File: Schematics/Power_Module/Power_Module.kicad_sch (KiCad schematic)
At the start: 0 parts

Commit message: Updates
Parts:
- added C1: 2.2n, symbol Device:C
- added C2, C3: 4.4u, symbol Device:C
- added C4, C5, C6: 0.1u, symbol Device:C
- added C7: 44u, symbol Device:C
- added C8, C9: 21u, symbol Device:C
- added D1, D2, D3: LED, symbol Device:LED
- added J1, J2, J3, J4: Screw_Terminal_01x02, symbol Connector:Screw_Terminal_01x02
- added L1: 6.8µ, symbol Device:L
- added L2: 5.6u, symbol Device:L
- added L3: 5.6µ, symbol Device:L
- added Q1, Q2: PMOS, symbol Simulation_SPICE:PMOS
- added R1: 44k, symbol Device:R_US
- added R2: 6k, symbol Device:R_US
- added R3, R5: 99k, symbol Device:R_US
- added R4, R6: 22k, symbol Device:R_US
- added R7: 150, symbol Device:R
- added R8, R9: 60, symbol Device:R
- added U1, U2, U3: LMR51430XDDCR, symbol QRET_Buck_PSU-symbols:LMR51430XDDCR
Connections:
- new net: C5.1, U2.6 (CB)
- new net: C5.2, L2.1, U2.2 (SW)
- new net: C6.2, L3.1, U3.2 (SW)
- new net: R5.2, R6.1, U3.4 (FB)
- new net: C6.1, U3.6 (CB)
- new net: J3.2 (Pin_2), J4.1 (Pin_1)
- new net: J3.1 (Pin_1), Q2.3 (S)
- new net: R1.2, R2.1, U1.4 (FB)
- new net: J1.1 (Pin_1), Q1.3 (S)
- new net: J1.2 (Pin_2), J2.1 (Pin_1)
- new net: R3.2, R4.1, U2.4 (FB)
- new net: D1.2 (A), R8.1
- new net: D2.2 (A), R7.1
- new net: C4.2, L1.1, U1.2 (SW)
- new net: D3.2 (A), R9.1
- new net: C4.1, U1.6 (CB)
- new net GND: C1.2, C2.2, C7.2, C8.2, D1.1 (K), D2.1 (K), J2.2 (Pin_2), Q1.2 (G), R2.2, R4.2, U1.1 (GND), U2.1 (GND)
- new net GND2: C3.2, C9.2, D3.1 (K), J4.2 (Pin_2), Q2.2 (G), R6.2, U3.1 (GND)
- new net Vbuck1: C8.1, L2.2, R3.1, R8.2
- new net Vbuck1.1: C7.1, L1.2, R1.1, R7.2
- new net Vbuck2: C9.1, L3.2, R5.1, R9.2
- new net Vin +: C1.1, C2.1, Q1.1 (D), U1.3 (VIN), U1.5 (EN), U2.3 (VIN), U2.5 (EN)
- new net Vin 2+: C3.1, Q2.1 (D), U3.3 (VIN), U3.5 (EN)
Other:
- note added: "Primary 3.3 V Buck Regulator"
- note added: "Primary 5.0 V Buck converter"
- note added: "Primary Power Connector"
- note added: "Secondary 3.3 V Buck Regulator"
- note added: "Secondary Power Connector"
- note added: "Vout = ((R1*0.6)/R2)+0.6"
- note added: "Vout = ((R3*0.6)/R4)+0.6"
- note added: "Vout = ((R5*0.6)/R6)+0.6"

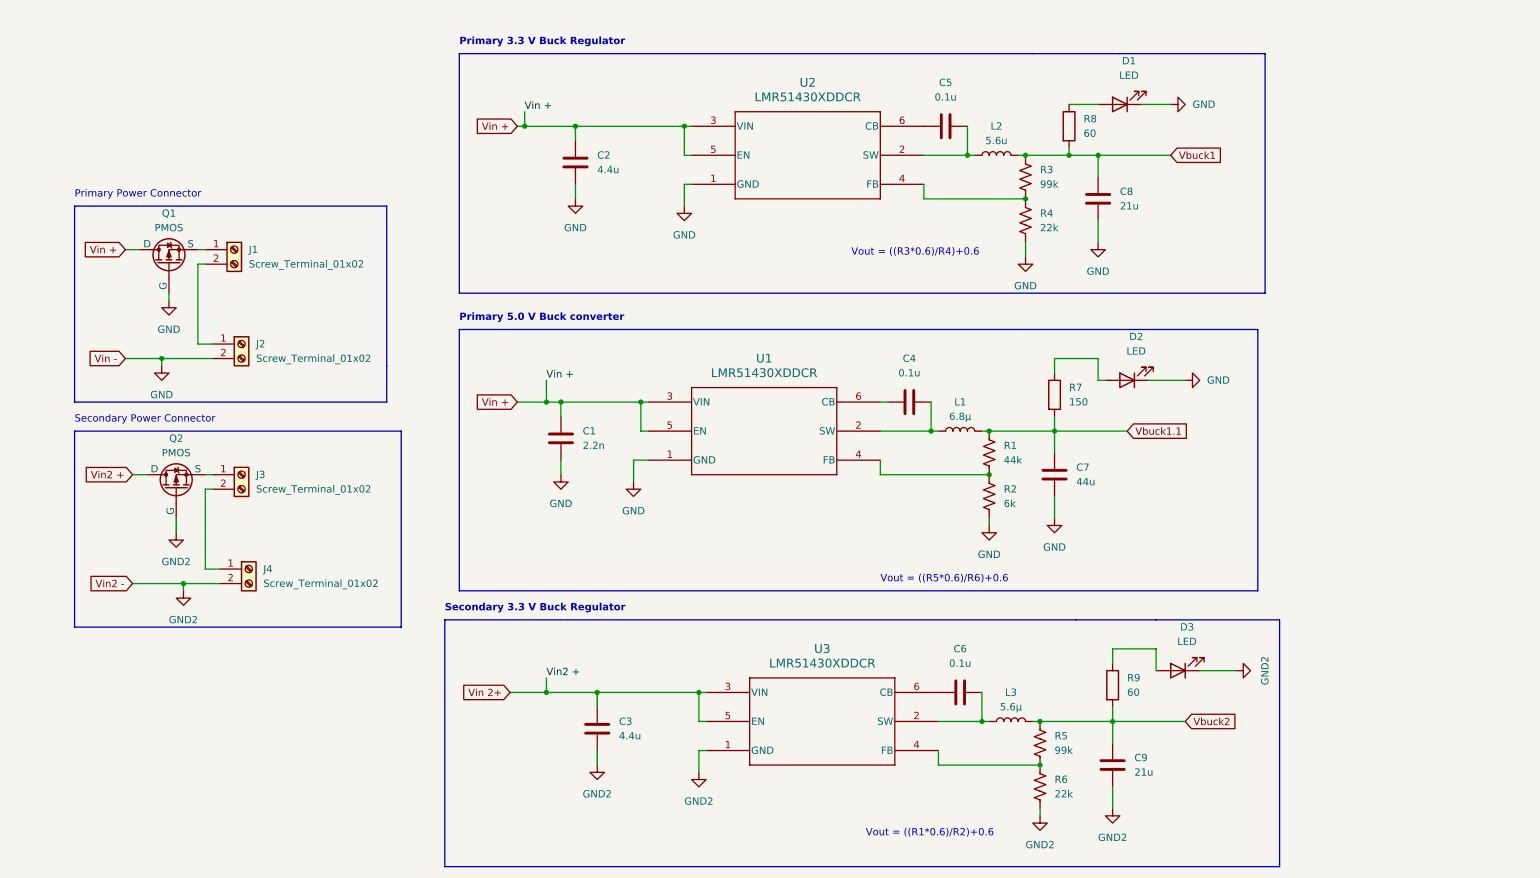
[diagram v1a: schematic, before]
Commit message: Added footprints
Added footprints
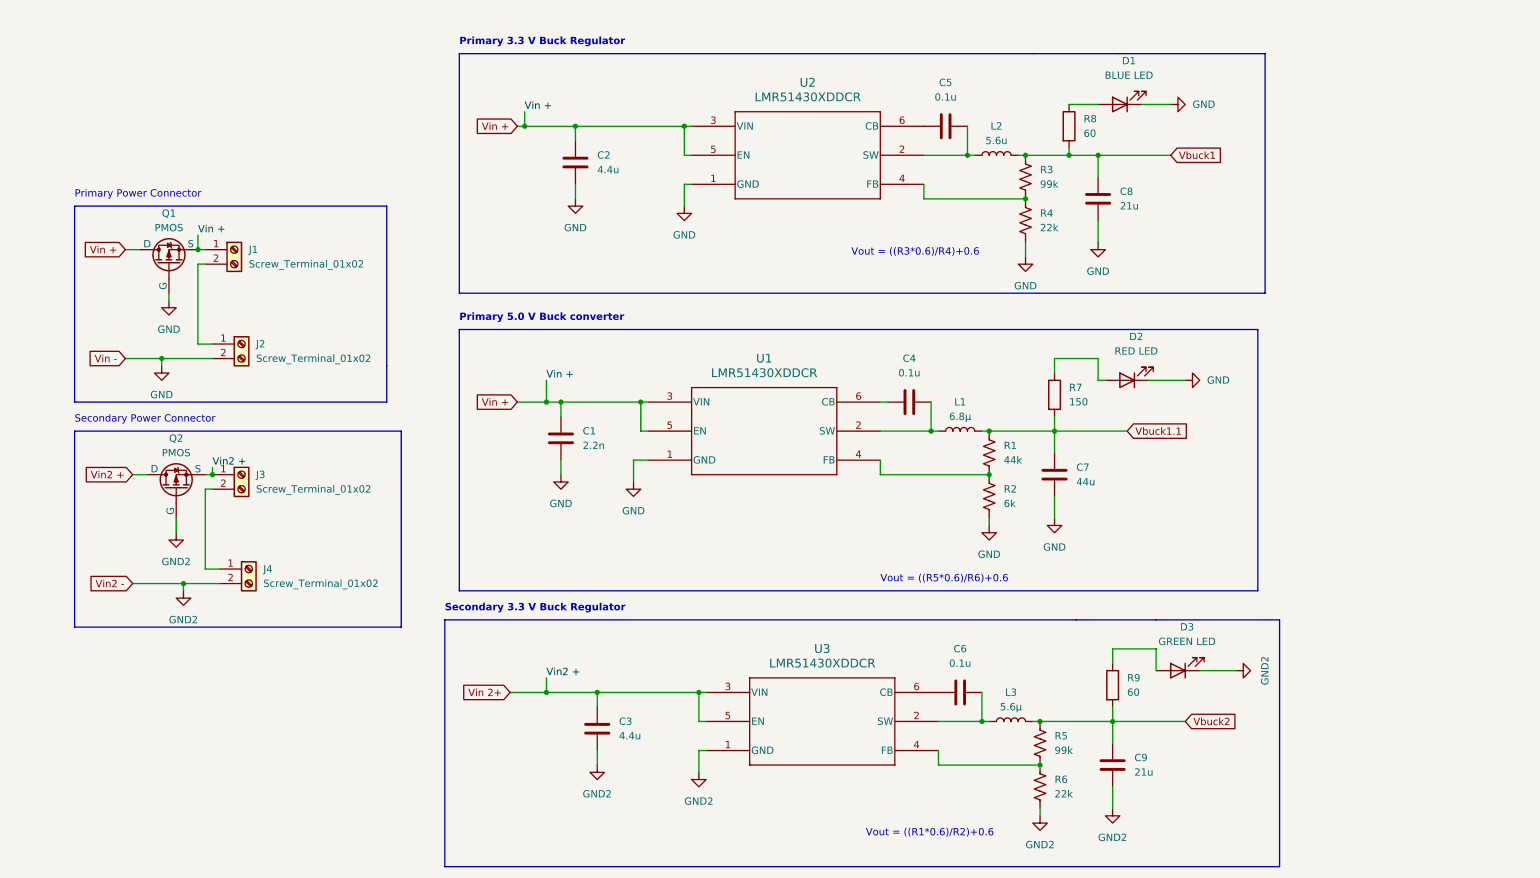
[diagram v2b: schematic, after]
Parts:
- C1, C2, C3, C4, C5, C6, C7, C8, C9: footprint (none) -> Capacitor_SMD:C_0201_0603Metric
- D1: value LED -> BLUE LED; footprint (none) -> LED_SMD:LED_0201_0603Metric
- D2: value LED -> RED LED; footprint (none) -> LED_SMD:LED_0201_0603Metric
- D3: value LED -> GREEN LED; footprint (none) -> LED_SMD:LED_0201_0603Metric
- J1, J2, J3, J4: footprint (none) -> TerminalBlock:TerminalBlock_Altech_AK300-2_P5.00mm
- L1, L2, L3: footprint (none) -> Inductor_SMD:L_0201_0603Metric
- Q1, Q2: footprint (none) -> footprints2:YJN3_TEX
- R1, R2, R3, R4, R5, R6, R7, R8, R9: footprint (none) -> Resistor_SMD:R_0201_0603Metric
- U1, U2, U3: footprint (none) -> footprints:SOT-23-THIN-6_DDC_TEX
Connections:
- net Vin +: now also J1.1 (Pin_1), Q1.3 (S)
- net Vin 2+: now also J3.1 (Pin_1), Q2.3 (S)

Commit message: Added LCSC part numbers
Added LCSC part numbers
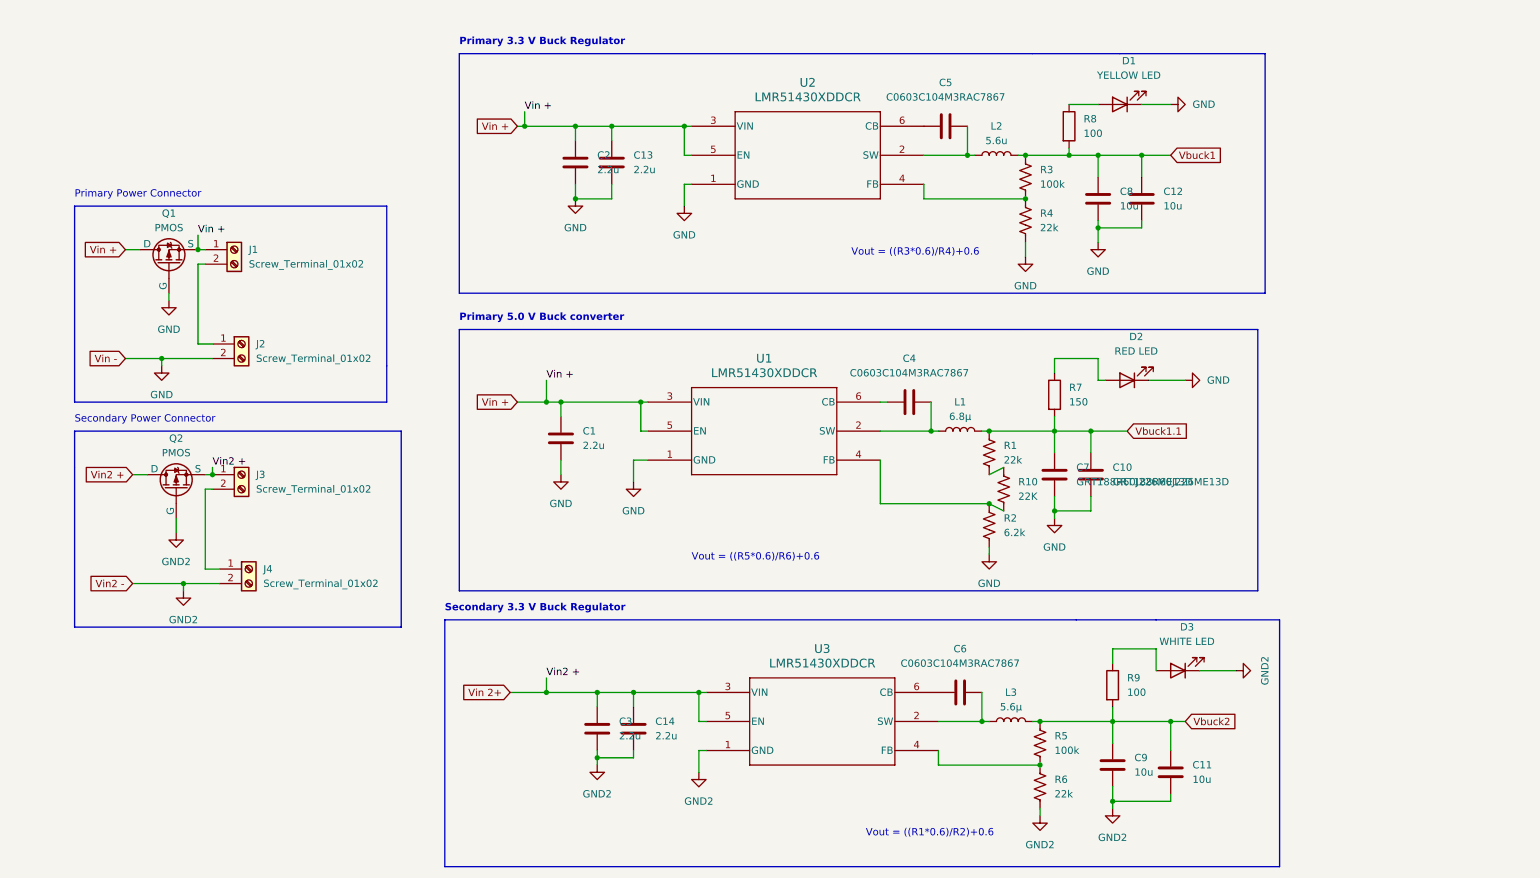
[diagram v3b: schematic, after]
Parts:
- added C10: GRT188R60J226ME13D, symbol Device:C
- added C11: 10u, Capacitor_SMD:C_0201_0603Metric, symbol Device:C
- added C12: 10u, symbol Device:C
- added C13, C14: 2.2u, symbol Device:C
- added R10: 22K, symbol Device:R_US
- C1: value 2.2n -> 2.2u; LCSC (none) -> C76612
- C2, C3: value 4.4u -> 2.2u; LCSC (none) -> C76612
- C4, C5, C6: value 0.1u -> C0603C104M3RAC7867
- C7: value 44u -> GRT188R60J226ME13D
- C8, C9: value 21u -> 10u; LCSC (none) -> C1952781
- D1: value BLUE LED -> YELLOW LED; LCSC (none) -> C2290
- D2: value RED LED -> RED LED; LCSC (none) -> C2286
- D3: value GREEN LED -> WHITE LED; LCSC (none) -> C2290
- L1: LCSC (none) -> C5137248
- L2, L3: LCSC (none) -> C5137243
- Q1, Q2: LCSC (none) -> C15127
- R1: value 44k -> 22k; LCSC (none) -> C31850
- R2: value 6k -> 6.2k; LCSC (none) -> C4260
- R3, R5: value 99k -> 100k; LCSC (none) -> C25803
- R4, R6: LCSC (none) -> C31850
- R7: LCSC (none) -> C22808
- R8, R9: value 60 -> 100; LCSC (none) -> C22775
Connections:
- net GND: now also C10.2, C12.2, C13.2
- net GND2: now also C11.2, C14.2
- net Vbuck1: now also C12.1
- net Vbuck1.1: now also C10.1
- net Vbuck2: now also C11.1
- net Vin +: now also C13.1
- net Vin 2+: now also C14.1
- net at R2.1, U1.4 (FB): now also R10.2; no longer R1.2
- new net: R1.2, R10.1
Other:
- moved on the sheet: R2

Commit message: All part numbers added + parallel caps and resistors removed
All part numbers added + parallel caps and resistors removed
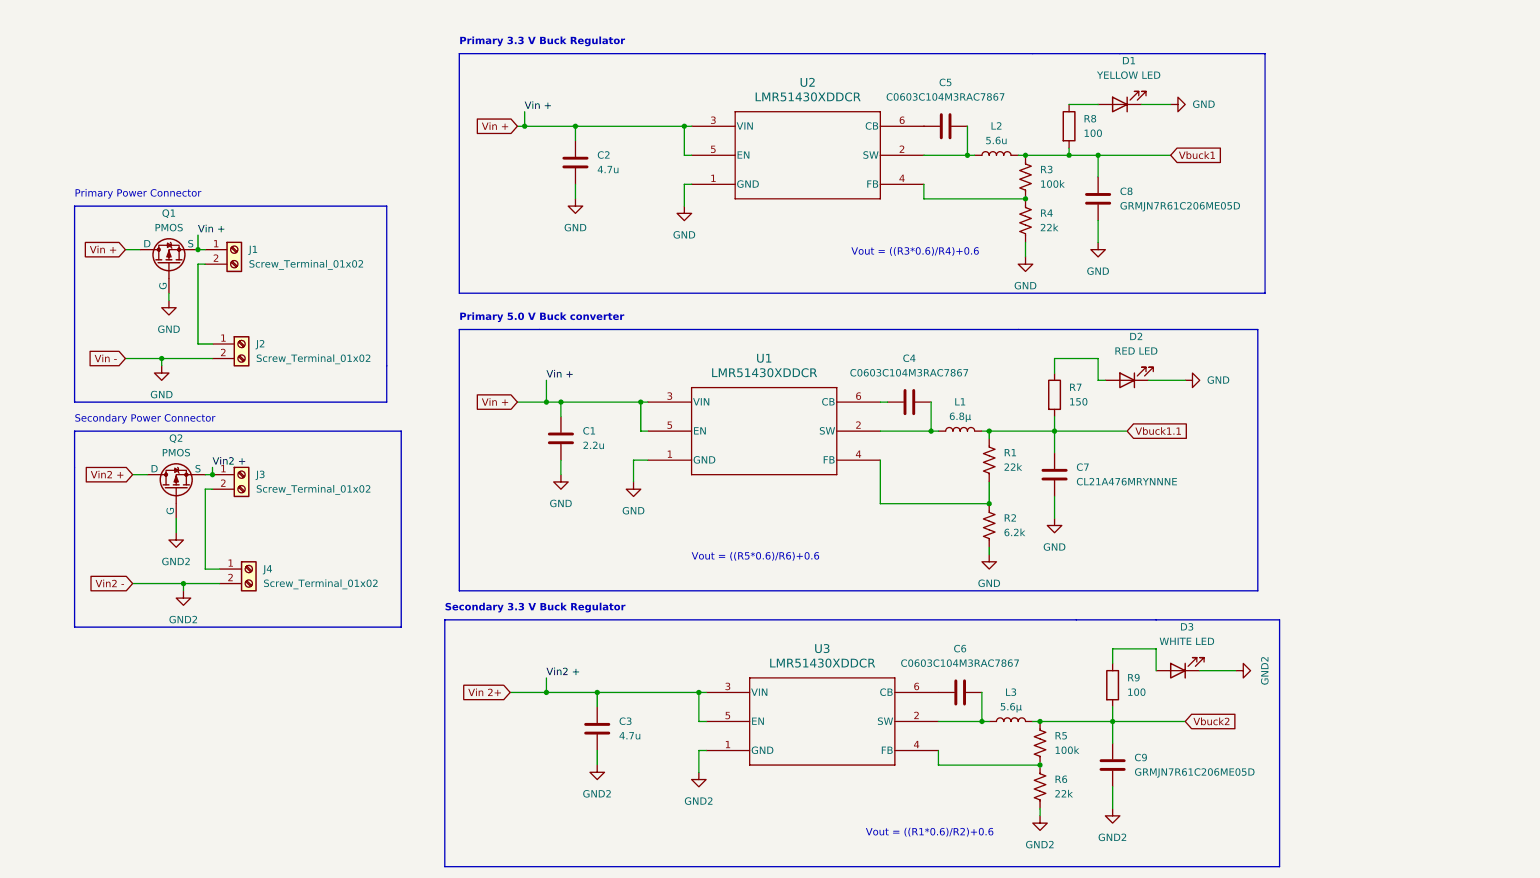
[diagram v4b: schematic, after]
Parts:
- removed C10: GRT188R60J226ME13D, symbol Device:C
- removed C11: 10u, Capacitor_SMD:C_0201_0603Metric, symbol Device:C
- removed C12: 10u, symbol Device:C
- removed C13, C14: 2.2u, symbol Device:C
- removed R10: 22K, symbol Device:R_US
- C2, C3: value 2.2u -> 4.7u; LCSC C76612 -> C71631
- C7: value GRT188R60J226ME13D -> CL21A476MRYNNNE
- C8, C9: value 10u -> GRMJN7R61C206ME05D; LCSC C1952781 -> (none)
- L3: LCSC C5137243 -> C139205
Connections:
- net at R2.1, U1.4 (FB): now also R1.2
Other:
- moved on the sheet: R1
